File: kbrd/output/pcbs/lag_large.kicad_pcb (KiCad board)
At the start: 2 copper layers, 163.6 x 165.5 mm, 76 parts

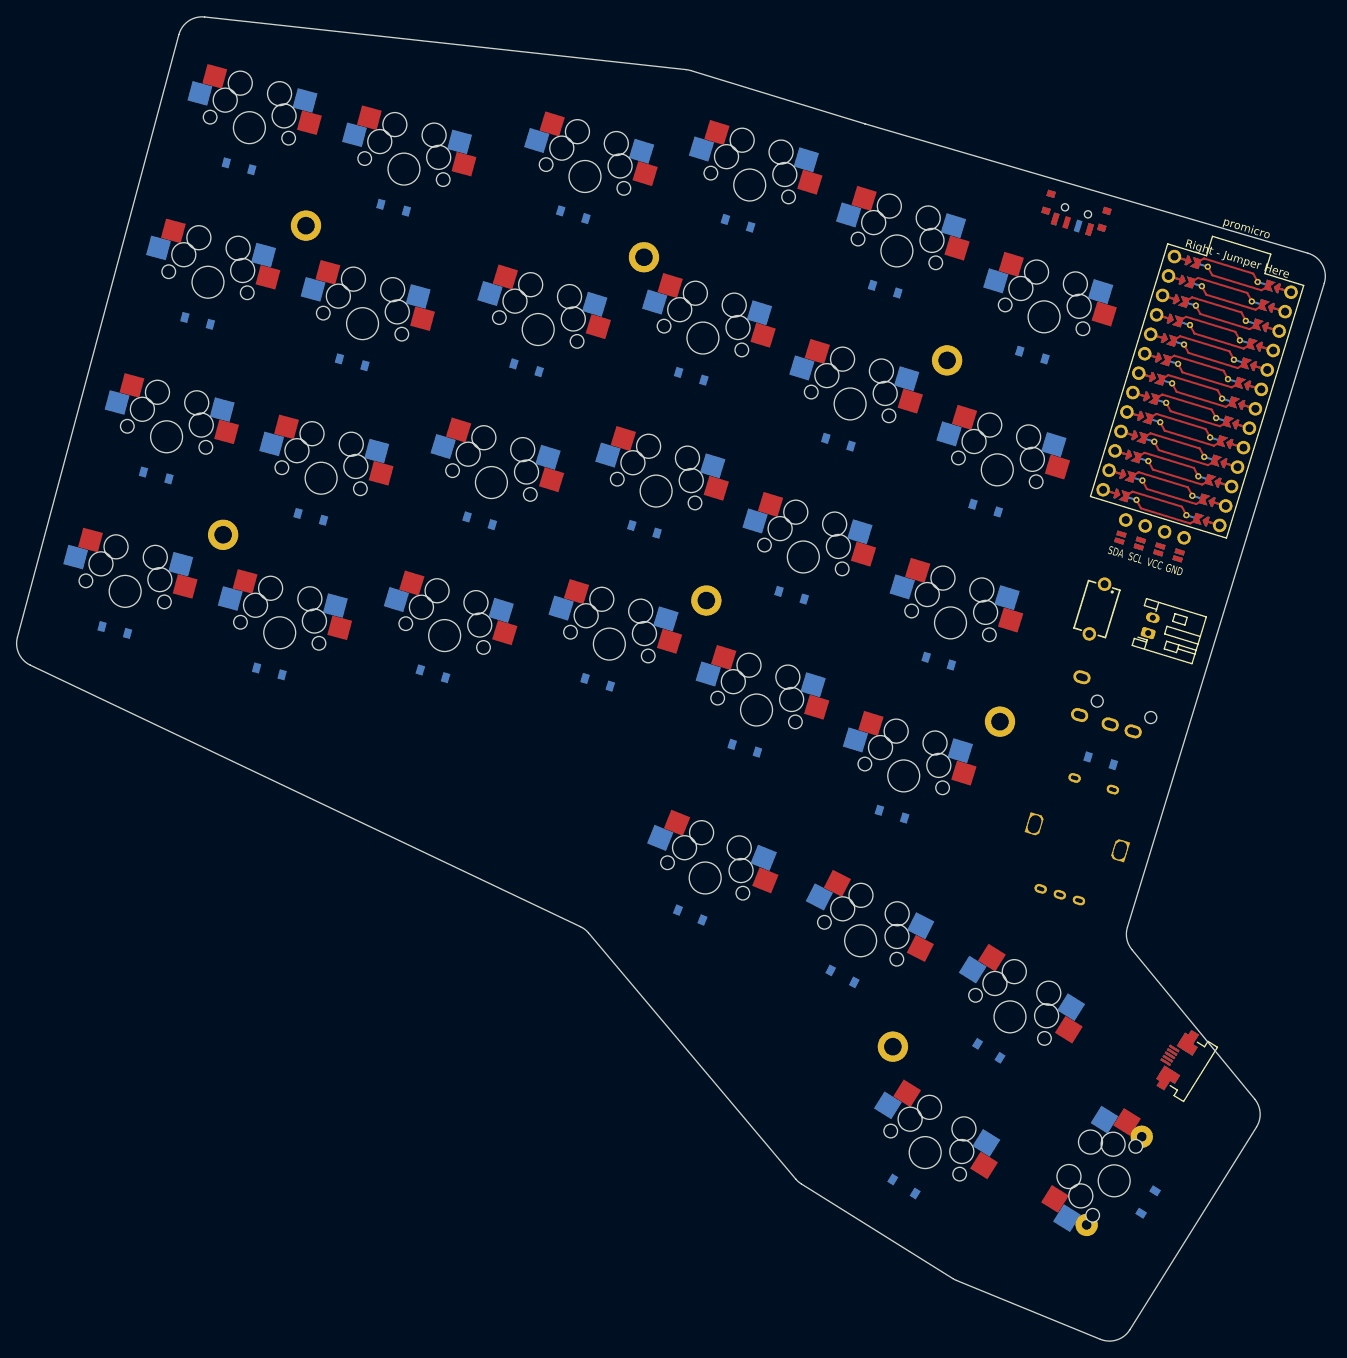
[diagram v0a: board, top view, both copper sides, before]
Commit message: footprint changes
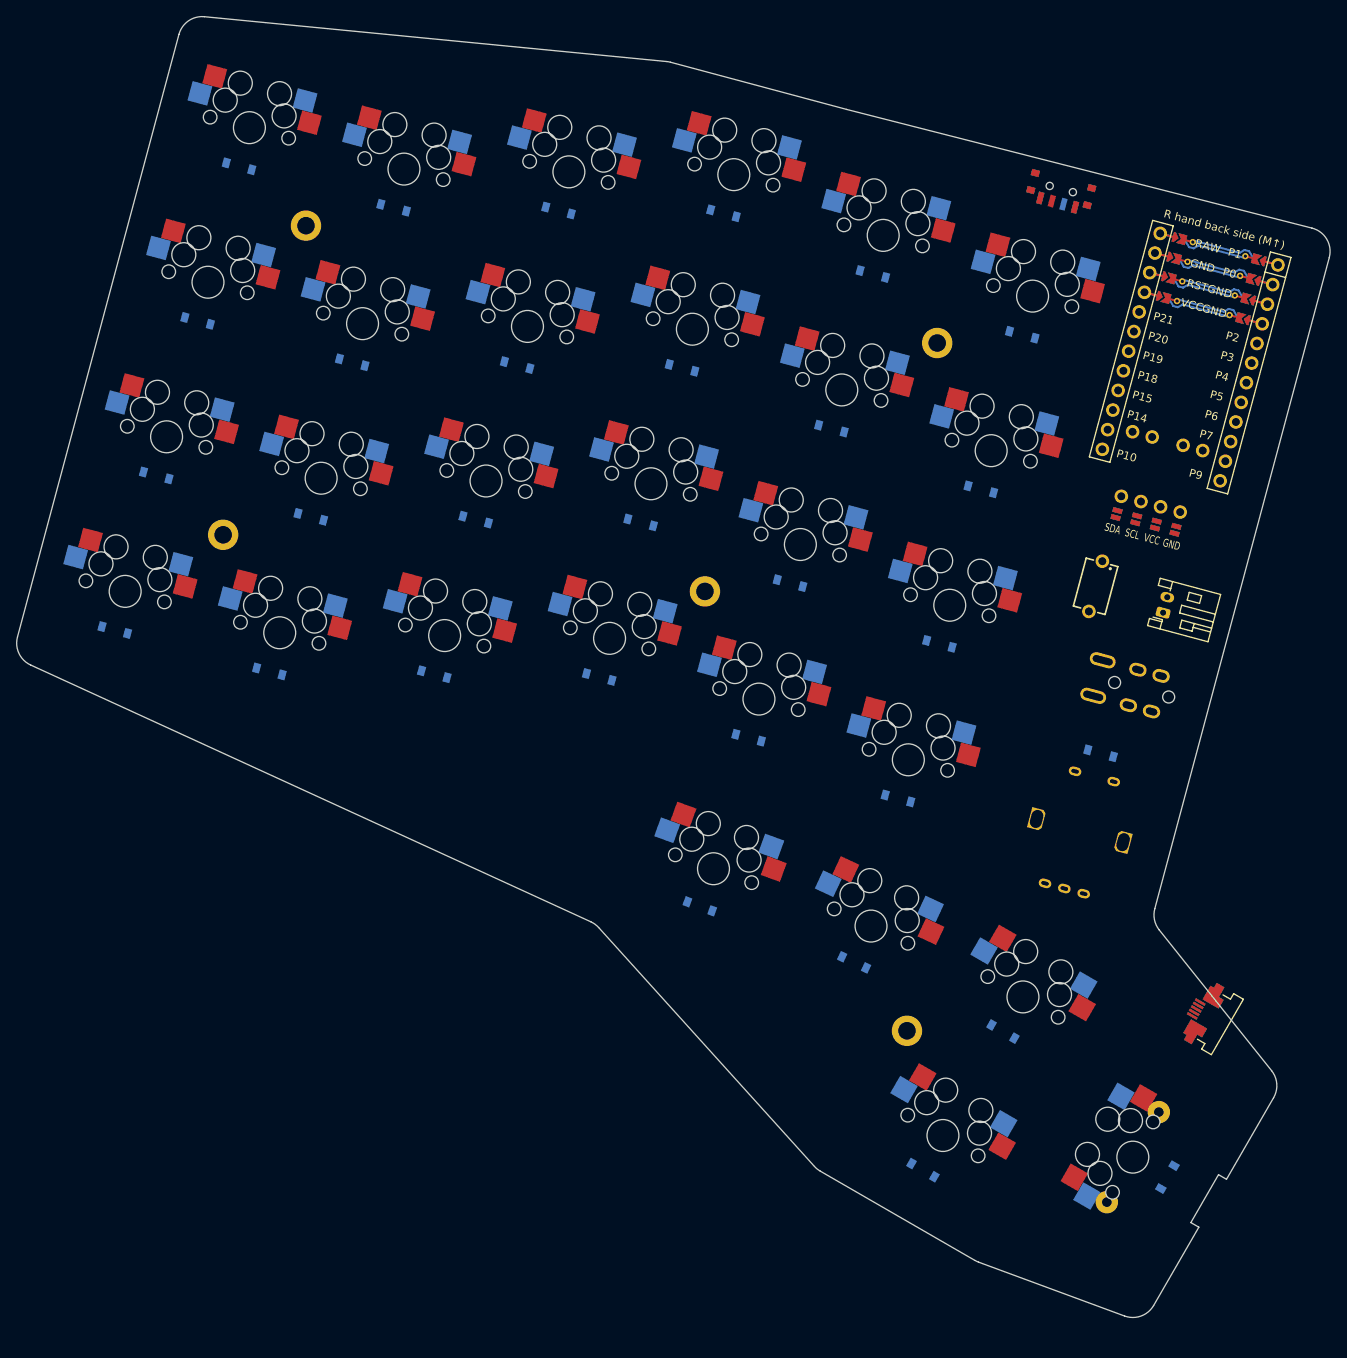
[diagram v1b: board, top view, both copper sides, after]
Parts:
- removed ?: , AMPHENOL_SFV5R-4STE1HLF
- removed ?: , ProMicro
- removed H8, H9: , ceoloide:mounting_hole_plated
- removed _2: , Connector_JST:JST_PH_S2B-PH-K_1x02_P2.00mm_Horizontal
- added MCU1: , ceoloide:mcu_supermini_nrf52840, F.Cu at (204.2, 92.0)
- added XX1: , AMPHENOL_SFV5R-4STE1HLF, F.Cu at (206.7, 175.9)
- added _1: , Connector_JST:JST_PH_S2B-PH-K_1x02_P2.00mm_Horizontal,  at (200.5, 125.1)
- TRRS1: footprint ceoloide:trrs_pj320a -> ceoloide:trrs_pj320a (reversible, symmetric)
- moved D29 3.94 mm to (201.0, 195.7), turned to 60 degrees
- moved H2 3.80 mm to (193.4, 198.8), turned to 60 degrees
- moved S29 3.77 mm to (196.7, 193.2), turned to 60 degrees
- moved H1 3.75 mm to (199.9, 187.6), turned to 60 degrees
- moved TRRS1 3.46 mm to (202.7, 136.1), turned to -105 degrees
- moved T1 3.31 mm to (187.6, 72.5), turned to 165 degrees
- moved D28 3.13 mm to (170.4, 194.8), turned to -30 degrees
- moved S28 3.08 mm to (172.9, 190.5), turned to -30 degrees
- moved D27 2.99 mm to (180.4, 177.5), turned to -30 degrees
- moved S27 2.98 mm to (182.9, 173.2), turned to -30 degrees
- moved S24 2.96 mm to (184.1, 85.6), turned to -15 degrees
- moved DISP1 2.93 mm to (194.6, 127.7), turned to 165 degrees
- moved S30 2.85 mm to (192.0, 121.8), turned to -105 degrees
- moved D24 2.84 mm to (182.8, 90.4), turned to -15 degrees
- moved H7 2.65 mm to (168.4, 177.4), turned to -27.5 degrees
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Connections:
- DISP1 pad 16: SCL -> P3
- DISP1 pad 17: SDA -> P2
- DISP1 pad 26: SCL -> P3
- DISP1 pad 27: SDA -> P2
- RE1 pad A: P0 -> P101
- RE1 pad C: P1 -> P102
- TRRS1 pad 3: (no net) -> P0
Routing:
- net (no net): track 371.5 -> 112.6 mm
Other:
- board size 163.6 x 165.5 mm -> 164.2 x 162.6 mm

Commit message: change joystick model
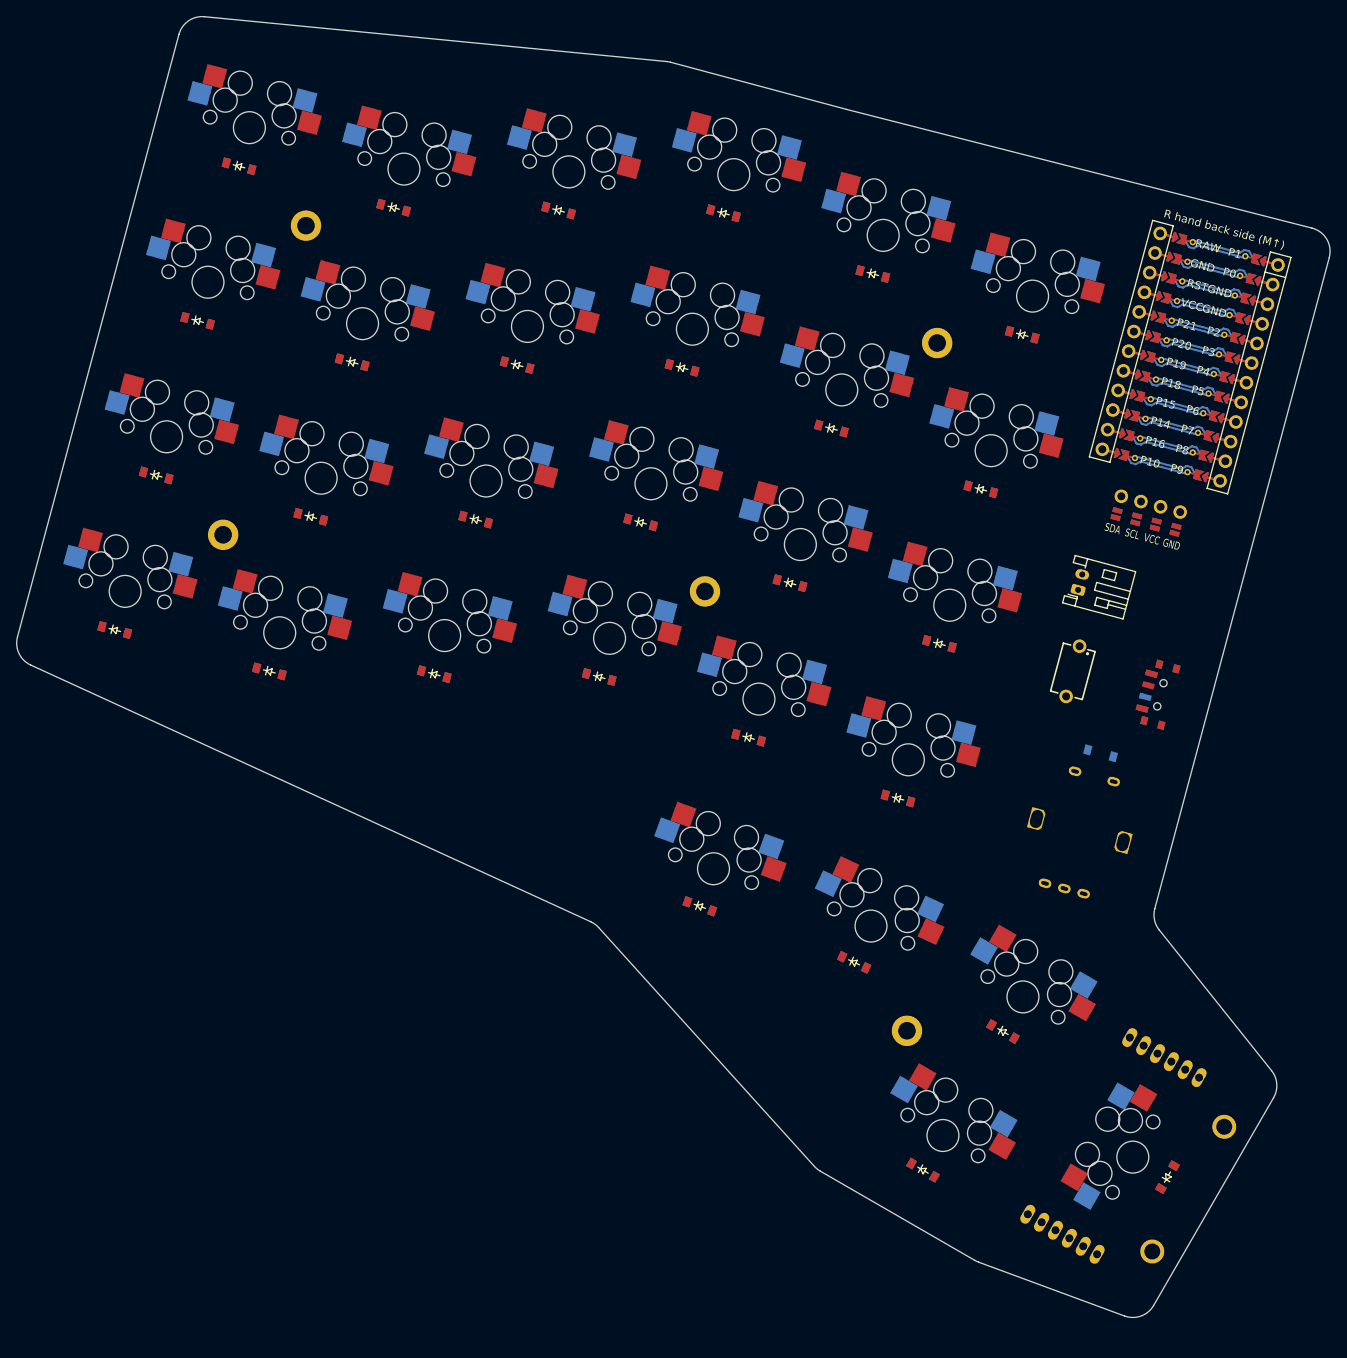
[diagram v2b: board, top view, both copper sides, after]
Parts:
- removed H6, H7: , ceoloide:mounting_hole_plated
- removed TRRS1: , ceoloide:trrs_pj320a (reversible, symmetric)
- added XX2: , joystick, F.Cu at (208.1, 189.4)
- D1, D10, D11, D12, D13, D14, D15, D16, D17, D18, D19, D2, D20, D21, D22, D23, D24, D25, D26, D27, D28, D29, D3, D4, D5, D6, D7, D8, D9: moved to F.Cu
- XX1: footprint AMPHENOL_SFV5R-4STE1HLF -> joystick
- moved H1 153.8 mm to (93.3, 76.8), turned to -15 degrees
- moved H2 109.5 mm to (172.2, 91.4), turned to -15 degrees
- moved H5 105.6 mm to (168.4, 177.4), turned to -27.5 degrees
- moved T1 64.0 mm to (199.8, 135.3), turned to 75 degrees
- moved H4 42.5 mm to (143.2, 122.5)
- moved H3 40.0 mm to (83.0, 115.4)
- moved XX1 30.1 mm to (199.1, 205.0)
- moved S30 11.0 mm to (189.2, 132.5)
- moved _1 11.0 mm to (189.8, 122.3)
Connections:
- MCU1 pad 10: P7 -> MCU1_10
- MCU1 pad 11: P8 -> MCU1_11
- MCU1 pad 12: P9 -> MCU1_12
- MCU1 pad 13: P10 -> MCU1_13
- MCU1 pad 14: P16 -> MCU1_14
- MCU1 pad 15: P14 -> MCU1_15
- MCU1 pad 16: P15 -> MCU1_16
- MCU1 pad 17: P18 -> MCU1_17
- MCU1 pad 18: P19 -> MCU1_18
- MCU1 pad 19: P20 -> MCU1_19
- MCU1 pad 20: P21 -> MCU1_20
- MCU1 pad 5: P2 -> MCU1_5
- MCU1 pad 6: P3 -> MCU1_6
- MCU1 pad 7: P4 -> MCU1_7
- MCU1 pad 8: P5 -> MCU1_8
- MCU1 pad 9: P6 -> MCU1_9
- RE1 pad A: P101 -> P0
- RE1 pad C: P102 -> P1
- XX1 pad 2: P20 -> GND
- XX1 pad 3: P19 -> P20
- XX1 pad 4: GND -> P19
- XX1 pad 5: P21 -> GND
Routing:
- net (no net): track 112.6 -> 337.7 mm
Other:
- outline, holes or cut-outs redrawn
